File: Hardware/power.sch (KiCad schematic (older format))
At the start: 66 parts, among them IC2 SIP32431DR3-T1GE3, IC3 SIP32431DR3-T1GE3, J2 614105150721, J3 B2B-XH-A, J4 POWER ON, Q2 FDC638P, Q3 IRLML6244TRPBF, Q4 BSS138, Q5 BSS138, Q8 BSS84AK,215, U10 TPS63900DSKR, U8 TP4056X

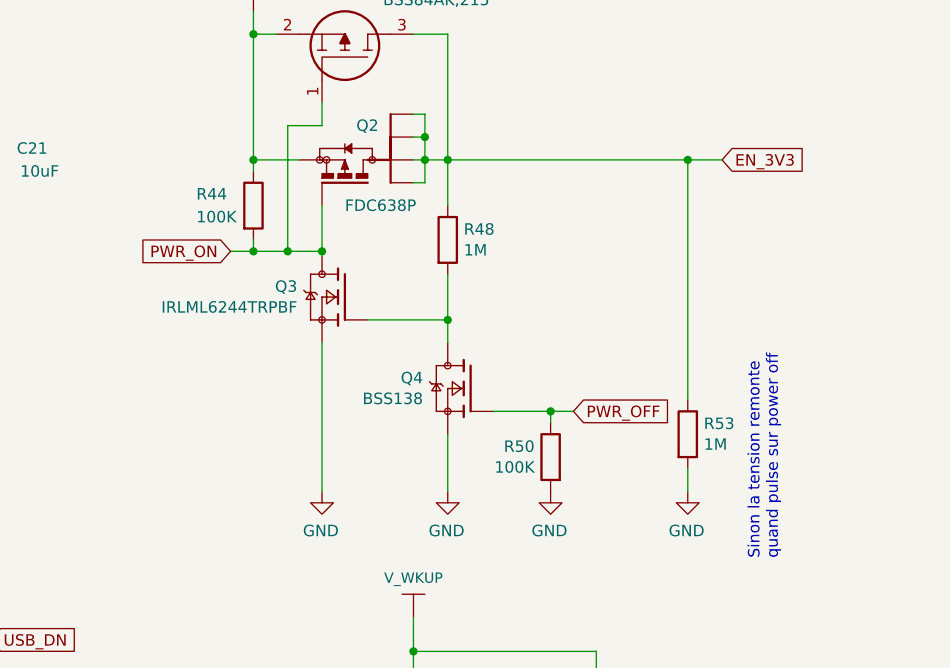
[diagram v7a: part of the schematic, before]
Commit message: Fix rtc write time, fix hx711 rate, Add offset for vbatt, start i2s dma mic
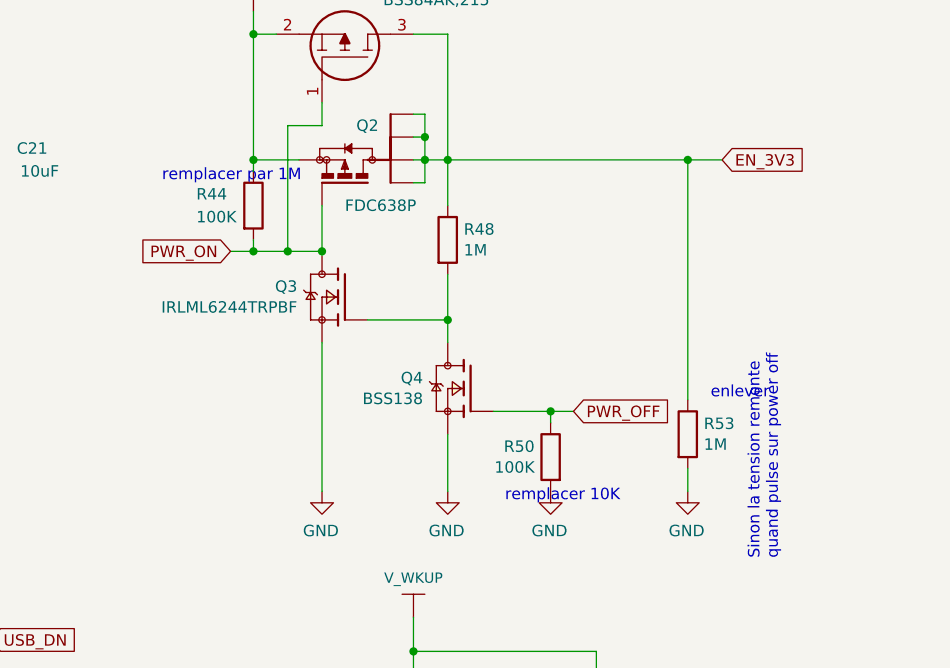
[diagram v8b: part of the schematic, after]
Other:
- note added: "enlever"
- note added: "remplacer 10K"
- note added: "remplacer par 1M"
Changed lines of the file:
@@
 Text Notes 6150 7200 0    50   ~ 0
 NM
+Text Notes 4450 4350 0    50   ~ 0
+remplacer par 1M
+Text Notes 5950 5750 0    50   ~ 0
+remplacer 10K
+Text Notes 6850 5300 0    50   ~ 0
+enlever
 $EndSCHEMATC
